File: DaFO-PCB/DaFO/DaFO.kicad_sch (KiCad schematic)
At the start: 33 parts, among them J1 HTSW-104-X-X-S, J2 CES-104-X-X-S, J3 1862042

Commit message: Actualización del README e información en el esquemático de la placa.
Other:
- company: (none) -> LabCES-Universidad de Costa Rica
- title: (none) -> Convertidor de digital a fibra óptica
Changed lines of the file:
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@@
 	(generator_version "9.0")
 	(paper "A4")
+	(title_block
+		(title "Convertidor de digital a fibra óptica")
+		(date "2026-02-09")
+		(rev "v.1")
+		(company "LabCES-Universidad de Costa Rica")
+	)
 	(text_box "Negar la señal o no"
 		(exclude_from_sim no)

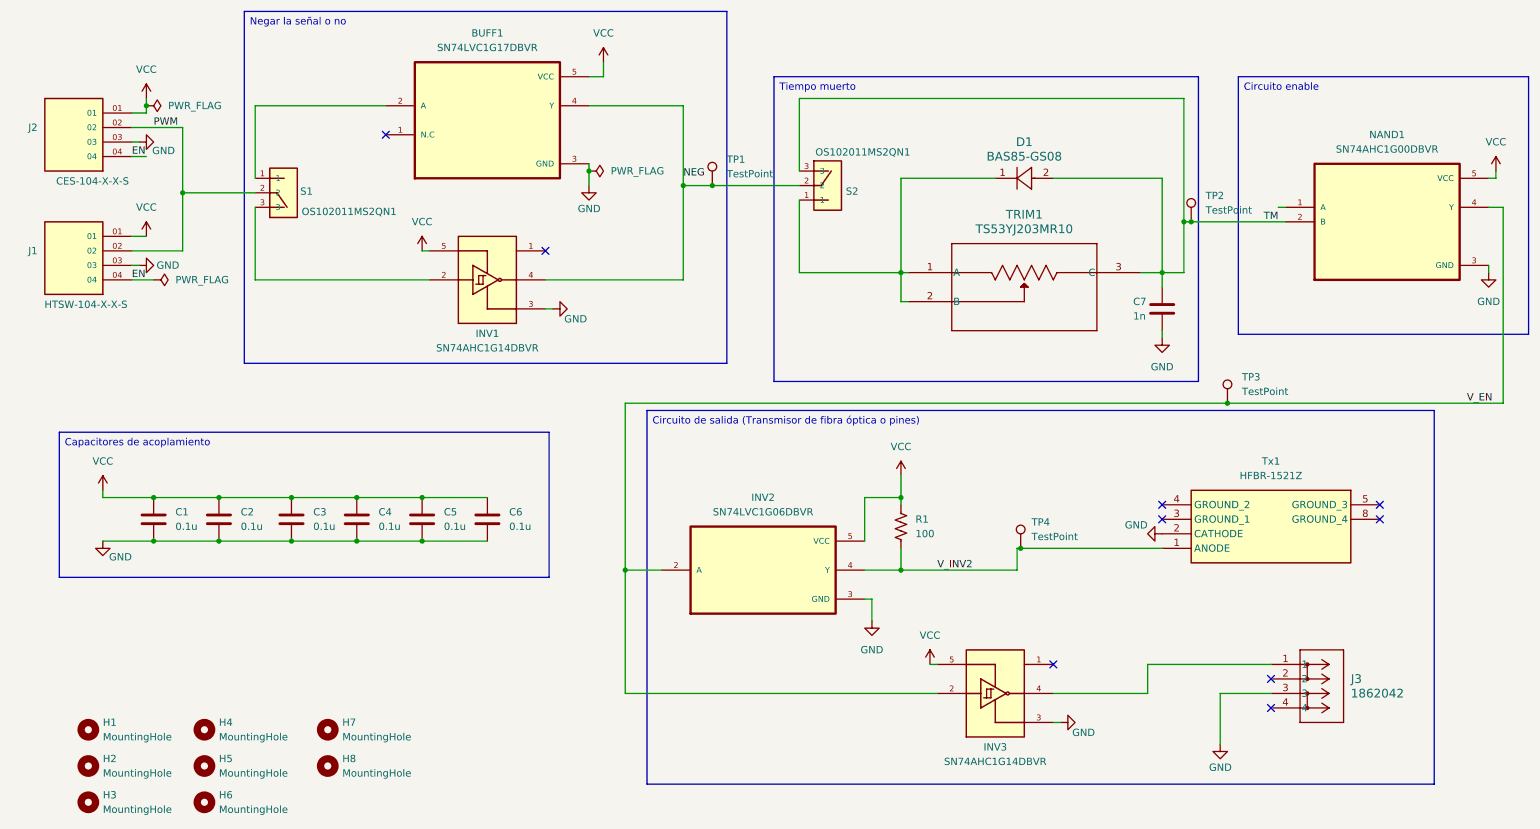
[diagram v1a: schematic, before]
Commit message: Cambios para reducir tamaño y a componentes laterales. Creación de archivos de fabricación.
Se realizaron cambios a la PCB para reducir su tamaño, se cambiaron ciertos componentes y se tienen los archivos de fabricación de la placa.
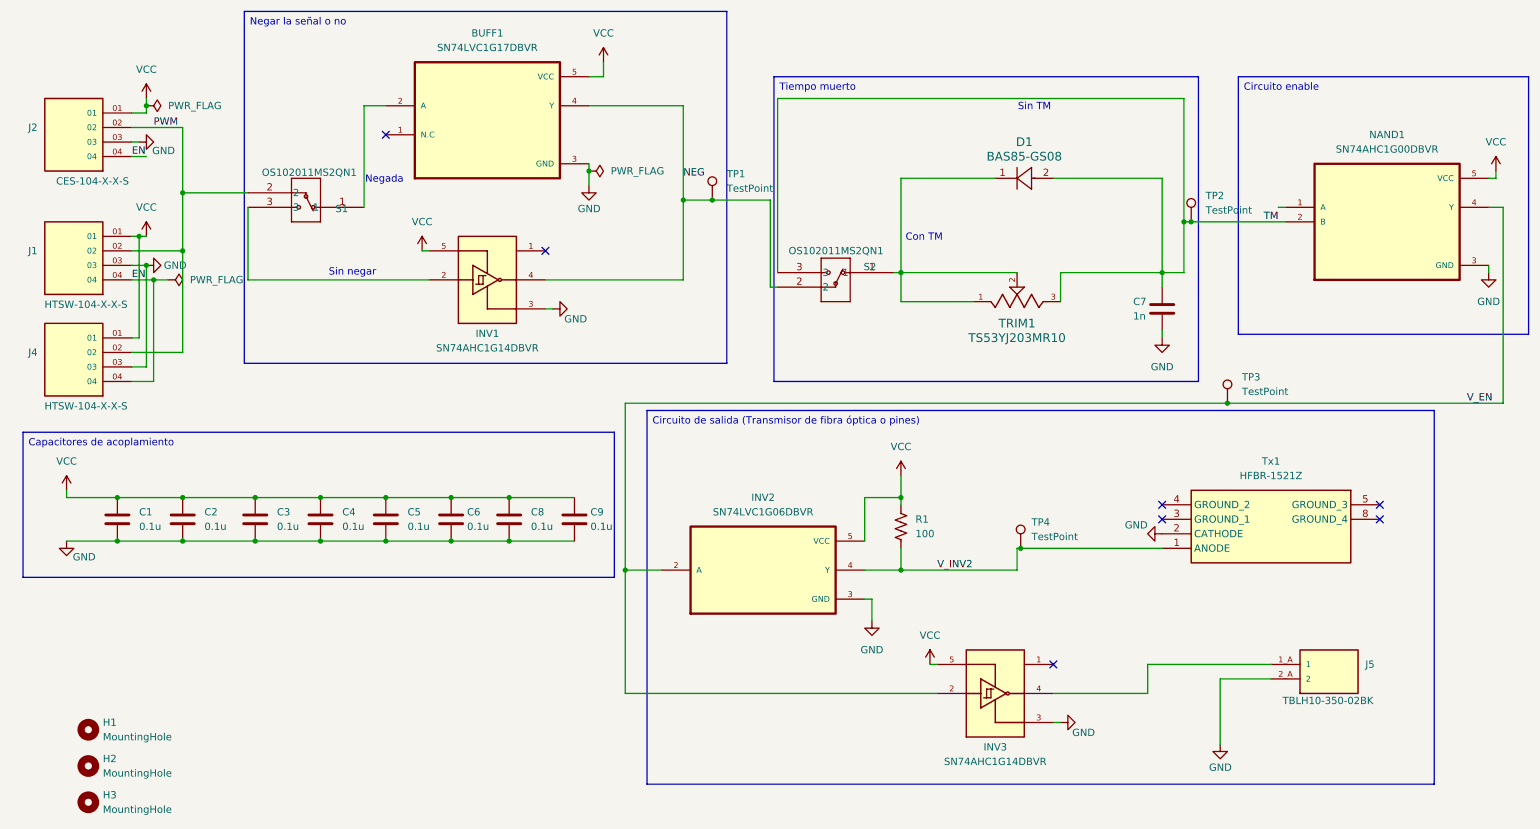
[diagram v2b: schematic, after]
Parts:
- removed H4, H5, H6, H7, H8: MountingHole, MountingHole:MountingHole_3.2mm_M3, symbol Mechanical:MountingHole
- removed J3: 1862042, CON_1862042:CONN_1862042, symbol CON_1862042:1862042
- added C8, C9: 0.1u, Capacitor_SMD:C_0603_1608Metric_Pad1.08x0.95mm_HandSolder, symbol Device:C
- added J4: HTSW-104-X-X-S, SAMTEC_HTSW-104-X-X-S:SAMTEC_HTSW-104-X-X-S, symbol HTSW-104-X-X-S:HTSW-104-X-X-S
- added J5: TBLH10-350-02BK, CON_TBLH10_350_02BK:CUI_TBLH10-350-02BK, symbol CON_TBLH10-350-02BK:TBLH10-350-02BK
- S1, S2: footprint SW_OS102011MS2QN1:SW_OS102011MS2QN1 -> SWITCH_OS102011MA1QN1:OS102011MA1QN1_CNK; symbol OS102011MS2QN1:OS102011MS2QN1 -> SWITCH_OS102011MA1QN1:OS102011MA1QN1
- TRIM1: footprint TS53YJ_VIS:TS53YJ_VIS -> TRIM_3214J:TRIM_3214J-1-203E; symbol TS53YJ_VIS:TS53YJ203MR10 -> TRIM_3214J-1-203E:3214J-1-203E; CREATOR (none) -> ANA; MANUFACTURER (none) -> Bourns; MAXIMUM_PACKAGE_HEIGHT (none) -> 3.71mm; PARTREV (none) -> 06/24; STANDARD (none) -> Manufacturer Recommendations; VERIFIER (none) -> NEZY
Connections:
- net EN: now also J4.04
- net GND: now also C8.2, C9.2, J4.03, J5.2_A (2)
- net PWM: now also J4.02
- net VCC: now also C8.1, C9.1, J4.01
- net at INV3.4: now also J5.1_A (1)
- no-connect marks 9 -> 7
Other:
- note added: "Con TM"
- note added: "Negada"
- note added: "Sin TM"
- note added: "Sin negar"
- moved on the sheet: C1, C2, C3, C4, C5, C6, TP1

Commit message: Actualización de archivo README.md
Adición de imágenes y cambio de estado del proyecto.
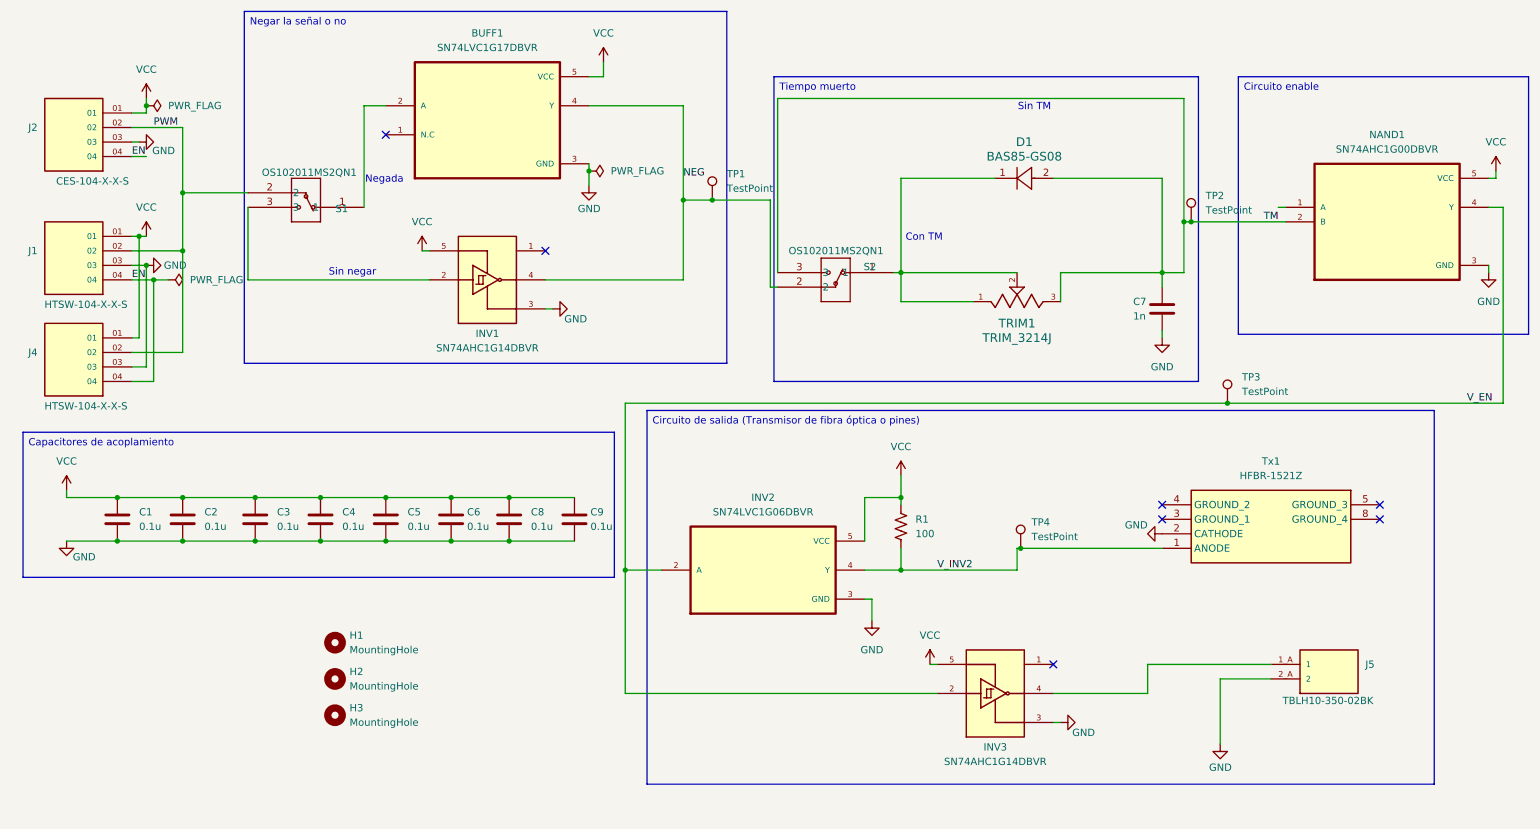
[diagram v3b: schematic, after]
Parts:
- TRIM1: value TS53YJ203MR10 -> TRIM_3214J
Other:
- moved on the sheet: H1, H2, H3
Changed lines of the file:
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@@
 	(title_block
 		(title "Convertidor de digital a fibra óptica")
-		(date "2026-05-20")
+		(date "2026-06-14")
 		(rev "v.1")
 		(company "LabCES-Universidad de Costa Rica")
@@
 			)
 		)
-		(property "Datasheet" ""
+		(property "Datasheet" "https://www.cuidevices.com/product/resource/tblh10-350.pdf"
 			(at 242.57 144.78 0)
 			(effects
@@
 			)
 		)
-		(property "Value" "TS53YJ203MR10"
+		(property "Value" "TRIM_3214J"
 			(at 187.96 85.09 0)
 			(effects
@@
 			)
 		)
-		(property "Datasheet" "https://www.vishay.com/doc?51008"
+		(property "Datasheet" "https://www.bourns.com/docs/Product-Datasheets/3214.pdf"
 			(at 187.96 78.74 0)
 			(effects
@@
 	(symbol
 		(lib_id "Mechanical:MountingHole")
-		(at 25.4 166.37 0)
+		(at 68.58 151.13 0)
 		(unit 1)
 		(exclude_from_sim no)
@@
 		(fields_autoplaced yes)
 		(property "Reference" "H3"
-			(at 27.94 165.0999 0)
+			(at 71.12 149.8599 0)
 			(effects
 				(font
@@
 		)
 		(property "Value" "MountingHole"
-			(at 27.94 167.6399 0)
+			(at 71.12 152.3999 0)
 			(effects
 				(font
@@
 		)
 		(property "Footprint" "MountingHole:MountingHole_3.2mm_M3"
-			(at 25.4 166.37 0)
+			(at 68.58 151.13 0)
 			(effects
 				(font
@@
 		)
 		(property "Datasheet" "~"
-			(at 25.4 166.37 0)
+			(at 68.58 151.13 0)
 			(effects
 				(font
@@
 		)
 		(property "Description" "Mounting Hole without connection"
-			(at 25.4 166.37 0)
+			(at 68.58 151.13 0)
 			(effects
 				(font
@@
 	(symbol
 		(lib_id "Mechanical:MountingHole")
-		(at 25.4 153.67 0)
+		(at 68.58 138.43 0)
 		(unit 1)
 		(exclude_from_sim no)
@@
 		(fields_autoplaced yes)
 		(property "Reference" "H1"
-			(at 27.94 152.3999 0)
+			(at 71.12 137.1599 0)
 			(effects
 				(font
@@
 		)
 		(property "Value" "MountingHole"
-			(at 27.94 154.9399 0)
+			(at 71.12 139.6999 0)
 			(effects
 				(font
@@
 		)
 		(property "Footprint" "MountingHole:MountingHole_3.2mm_M3"
-			(at 25.4 153.67 0)
+			(at 68.58 138.43 0)
 			(effects
 				(font
@@
 		)
 		(property "Datasheet" "~"
-			(at 25.4 153.67 0)
+			(at 68.58 138.43 0)
 			(effects
 				(font
@@
 		)
 		(property "Description" "Mounting Hole without connection"
-			(at 25.4 153.67 0)
+			(at 68.58 138.43 0)
 			(effects
 				(font
@@
 	(symbol
 		(lib_id "Mechanical:MountingHole")
-		(at 25.4 160.02 0)
+		(at 68.58 144.78 0)
 		(unit 1)
 		(exclude_from_sim no)
@@
 		(fields_autoplaced yes)
 		(property "Reference" "H2"
-			(at 27.94 158.7499 0)
+			(at 71.12 143.5099 0)
 			(effects
 				(font
@@
 		)
 		(property "Value" "MountingHole"
-			(at 27.94 161.2899 0)
+			(at 71.12 146.0499 0)
 			(effects
 				(font
@@
 		)
 		(property "Footprint" "MountingHole:MountingHole_3.2mm_M3"
-			(at 25.4 160.02 0)
+			(at 68.58 144.78 0)
 			(effects
 				(font
@@
 		)
 		(property "Datasheet" "~"
-			(at 25.4 160.02 0)
+			(at 68.58 144.78 0)
 			(effects
 				(font
@@
 		)
 		(property "Description" "Mounting Hole without connection"
-			(at 25.4 160.02 0)
+			(at 68.58 144.78 0)
 			(effects
 				(font
